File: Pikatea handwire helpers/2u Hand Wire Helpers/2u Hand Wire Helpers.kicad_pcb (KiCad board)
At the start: 2 copper layers, 29.2 x 20.1 mm, 3 parts

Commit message: update andwire gerbers
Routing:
- net Net-(D1-Pad2): track 25.3 -> 26.5 mm

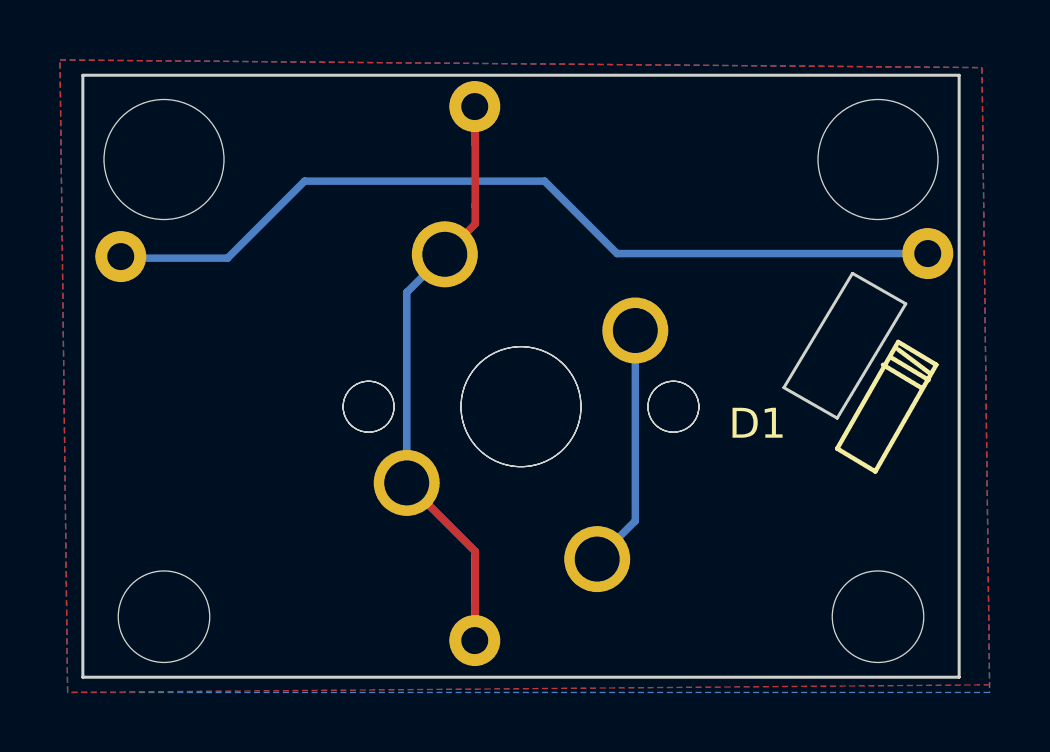
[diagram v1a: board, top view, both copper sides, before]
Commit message: update handwire helpers
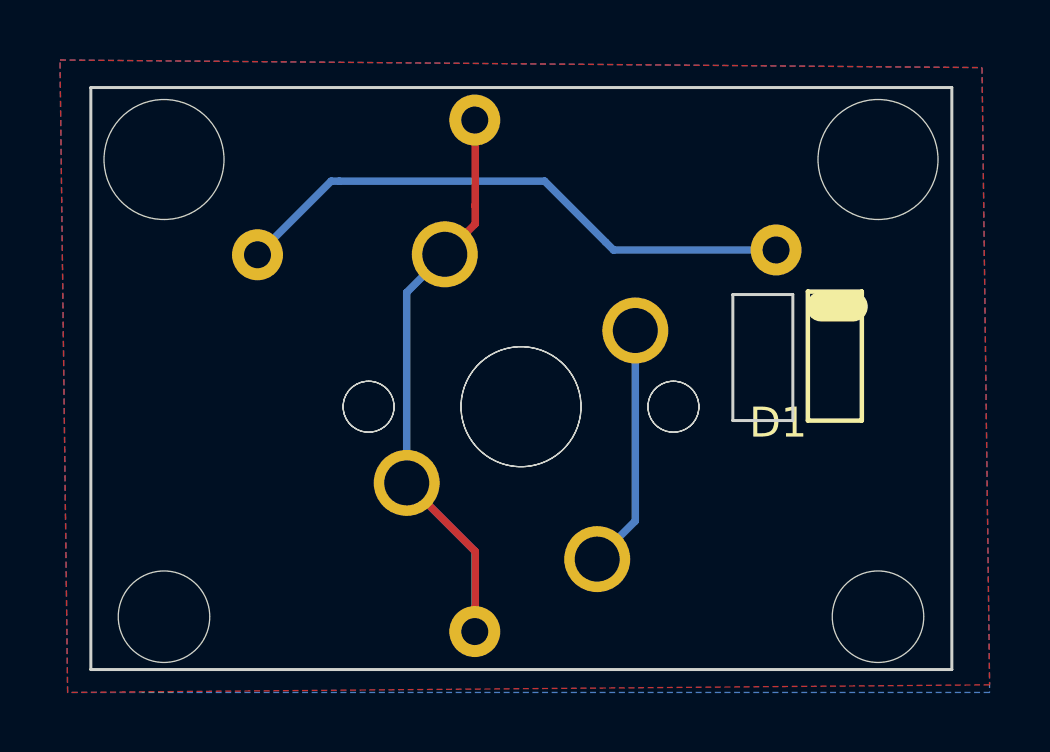
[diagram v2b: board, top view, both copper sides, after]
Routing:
- net Net-(D1-Pad1): track 29.0 -> 19.3 mm
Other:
- board size 29.2 x 20.1 mm -> 28.7 x 19.4 mm
- net class Default removed
